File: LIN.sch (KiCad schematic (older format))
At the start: 10 parts

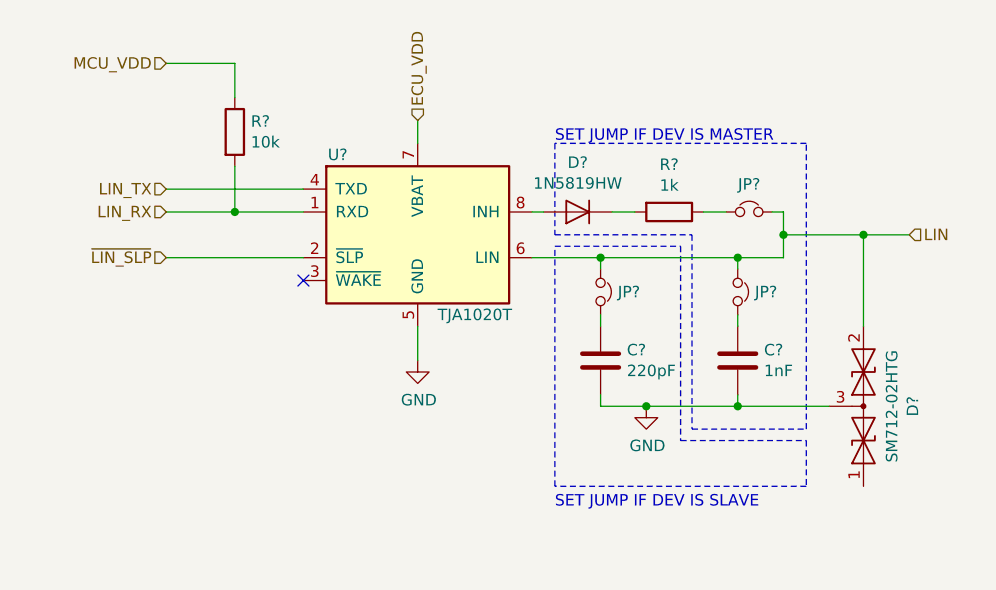
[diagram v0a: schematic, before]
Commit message: corrected CAN schematic
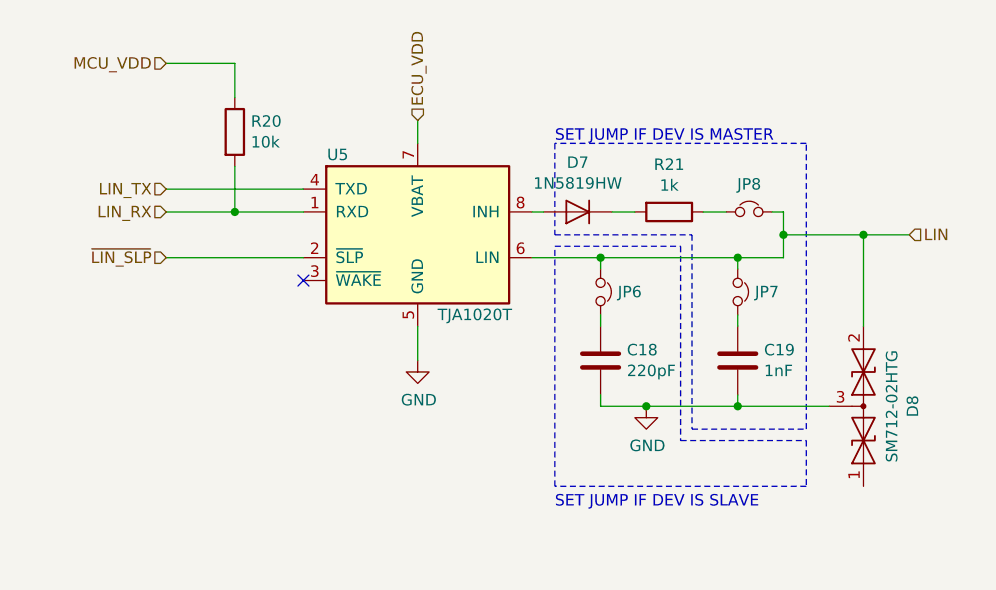
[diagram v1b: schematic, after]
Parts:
- C13: renamed from C?; footprint Capacitor_SMD:C_0805_2012Metric -> Capacitor_SMD:C_0603_1608Metric; Description (none) -> 220pF ±10% 50V X7R 0603 Multilayer Ceramic Capacitors; Manufacturer (none) -> Samsung Electro-Mechanics; Mount (none) -> MOUNT; MountType (none) -> SMD; PartNumber (none) -> CL10B221KB8NNNC
- C14: renamed from C?; footprint Capacitor_SMD:C_0805_2012Metric -> Capacitor_SMD:C_0603_1608Metric; Description (none) -> 1nF ±10% 50V X7R 0603 Multilayer Ceramic Capacitors; Manufacturer (none) -> Samsung Electro-Mechanics; Mount (none) -> MOUNT; MountType (none) -> SMD; PartNumber (none) -> CL10B102KB8NNNC
- D4: renamed from D?; Description (none) -> 40V 1A 450mV @ 1A SOD-123 Schottky Barrier Diodes (SBD) RoHS; Manufacturer (none) -> Diodes Incorporated Completes; Mount (none) -> MOUNT; MountType (none) -> SMD; PartNumber (none) -> 1N5819HW-7-F
- D5: renamed from D?; Description (none) -> Bidirectional 12V 13.3V 31V 19A (8/20us) SOT-23(SOT-23-3) T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; Manufacturer (none) -> Littelfuse; Mount (none) -> MOUNT; MountType (none) -> SMD; PartNumber (none) -> SM712-02HTG
- JP1, JP2, JP3: renamed from JP?; Description (none) -> NOT A COMPONENT; Manufacturer (none) -> NOT A COMPONENT; Mount (none) -> DO NOT MOUNT; MountType (none) -> SMD; PartNumber (none) -> NOT A COMPONENT
- R16: renamed from R?; footprint Resistor_SMD:R_0805_2012Metric -> Resistor_SMD:R_0603_1608Metric; Manufacturer (none) -> -; Mount (none) -> MOUNT; MountType (none) -> SMD
- R17: renamed from R?; Manufacturer (none) -> -; Mount (none) -> MOUNT; MountType (none) -> SMD
- U3: renamed from U?; Description (none) -> LIN transceiver RoHS; Manufacturer (none) -> NXP; Mount (none) -> MOUNT; MountType (none) -> SMD; PartNumber (none) -> TJA1020T/CM,118

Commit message: Start routing
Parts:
- R16: Description (none) -> 10K ±5% 1/10W ±100ppm/℃ 0603 Chip Resistor - Surface Mount; Manufacturer - -> YAGEO; PartNumber (none) -> RC0603JR-0710KL
- R17: Description (none) -> 1kΩ ±1% 0.1W ±100ppm/℃ 0603 Chip Resistor - Surface Mount R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; Manufacturer - -> YAGEO; PartNumber (none) -> RC0603FR-071KL
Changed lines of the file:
@@
 F 1 "1k" V 6234 4250 50  0000 C CNN
 F 2 "Resistor_SMD:R_0805_2012Metric" V 6280 4250 50  0001 C CNN
-F 3 "~" H 6350 4250 50  0001 C CNN
+F 3 "https://datasheet.lcsc.com/szlcsc/YAGEO-RC0603FR-071KL_C22548.pdf" H 6350 4250 50  0001 C CNN
 F 4 "MOUNT" H 6350 4250 50  0001 C CNN "Mount"
 F 5 "SMD" H 6350 4250 50  0001 C CNN "MountType"
-F 6 "-" H 6350 4250 50  0001 C CNN "Manufacturer"
+F 6 "YAGEO" H 6350 4250 50  0001 C CNN "Manufacturer"
+F 7 "1kΩ ±1% 0.1W ±100ppm/℃ 0603 Chip Resistor - Surface Mount RoHS" H 6350 4250 50  0001 C CNN "Description"
+F 8 "RC0603FR-071KL" H 6350 4250 50  0001 C CNN "PartNumber"
 	1    6350 4250
 	0    1    1    0
@@
 F 1 "10k" H 4520 3855 50  0000 L CNN
 F 2 "Resistor_SMD:R_0603_1608Metric" V 4380 3900 50  0001 C CNN
-F 3 "~" H 4450 3900 50  0001 C CNN
+F 3 "https://datasheet.lcsc.com/szlcsc/1811081617_YAGEO-RC0603JR-0710KL_C99198.pdf" H 4450 3900 50  0001 C CNN
 F 4 "MOUNT" H 4450 3900 50  0001 C CNN "Mount"
 F 5 "SMD" H 4450 3900 50  0001 C CNN "MountType"
-F 6 "-" H 4450 3900 50  0001 C CNN "Manufacturer"
+F 6 "YAGEO" H 4450 3900 50  0001 C CNN "Manufacturer"
+F 7 "10K ±5% 1/10W ±100ppm/℃ 0603 Chip Resistor - Surface Mount" H 4450 3900 50  0001 C CNN "Description"
+F 8 "RC0603JR-0710KL" H 4450 3900 50  0001 C CNN "PartNumber"
 	1    4450 3900
 	1    0    0    -1

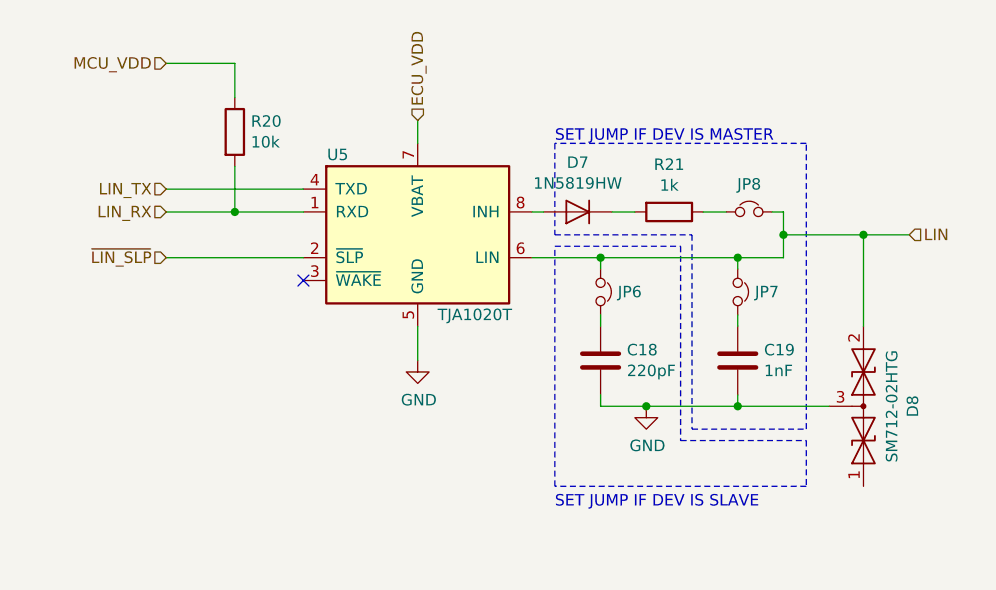
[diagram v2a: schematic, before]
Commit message: CAN part routing
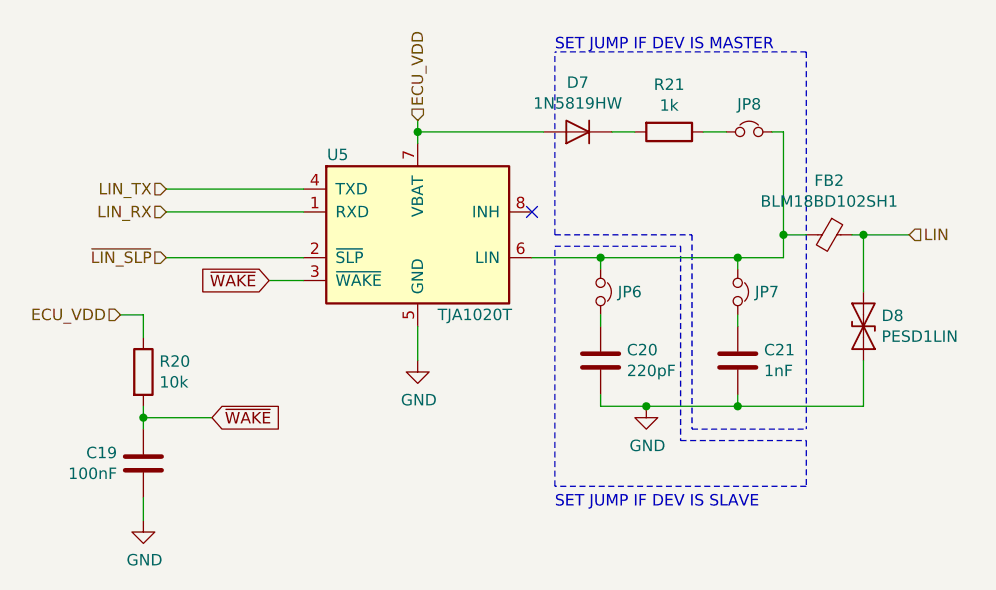
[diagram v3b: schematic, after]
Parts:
- removed D5: SM712-02HTG, Package_TO_SOT_SMD:SOT-23, symbol Device:D_TVS_x2_AAC
- added C13: 100nF, Capacitor_SMD:C_0603_1608Metric, symbol Device:C
- added D8: PESD1LIN, Diode_SMD:D_SOD-323, symbol Device:D_TVS
- added FB2: BLM18BD102SH1, Inductor_SMD:L_0603_1608Metric, symbol Device:Ferrite_Bead_Small
- JP1, JP2, JP3: footprint Connector_PinHeader_2.54mm:PinHeader_1x02_P2.54mm_Vertical -> Jumper:SolderJumper-2_P1.3mm_Open_RoundedPad1.0x1.5mm
- renumbered C13 to C14, C14 to C15
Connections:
- net MCU_VDD is gone; now on net ECU_VDD: R16.1
- net ECU_VDD: now also D4.2 (A)
- net GND: now also C13.2, D8.2 (A2)
- net LIN: now also D8.1 (A1), FB2.1; no longer JP1.1, JP2.1, JP3.2, U3.6 (LIN)
- net LIN_RX: no longer R16.2
- net at U3.8 (INH): no longer D4.2 (A)
- net ~WAKE: now reaches U3.3 (~WAKE~)
- net ~WAKE: now also R16.2, C13.1
- new net: FB2.2, JP1.1, JP2.1, JP3.2, U3.6 (LIN)
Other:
- moved on the sheet: D7, JP8, R21
